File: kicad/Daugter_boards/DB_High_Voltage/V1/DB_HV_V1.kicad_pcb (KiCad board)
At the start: 2 copper layers, 57.2 x 50.8 mm, 38 parts, among them P1 CONN_01X19, P2 CONN_01X02, P3 CONN_01X19, P4 SMA, Q1 QN2222, Q2 QN2222, Q3 Q2N2907, U1 LM555N

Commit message: update DB_HV, update librairy and librairy path for MDL
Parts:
- Q1, Q2: value QN2222 -> Q2N2222
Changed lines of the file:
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@@
     (links 66)
     (no_connects 0)
-    (area 71.044999 30.526666 131.905 90.835001)
+    (area 71.044999 32.944999 128.345001 83.895001)
     (thickness 1.6)
     (drawings 4)
@@
     (pad_to_mask_clearance 0.2)
     (aux_axis_origin 0 0)
-    (visible_elements FFFFFF7F)
+    (visible_elements 7FFFFFFF)
     (pcbplotparams
       (layerselection 0x00030_80000001)
@@
       (effects (font (size 1 1) (thickness 0.15)))
     )
-    (fp_text value QN2222 (at 0 4.826 90) (layer F.Fab)
+    (fp_text value Q2N2222 (at 0 4.826 90) (layer F.Fab)
       (effects (font (size 1 1) (thickness 0.15)))
     )
@@
       (effects (font (size 1 1) (thickness 0.15)))
     )
-    (fp_text value QN2222 (at 0 4.826 90) (layer F.Fab)
-      (effects (font (size 1 1) (thickness 0.15)))
-    )
+    (fp_text value Q2N2222 (at 0 4.826 90) (layer F.Fab)
+      (effects (font (size 1 1) (thickness 0.15)))
+    )

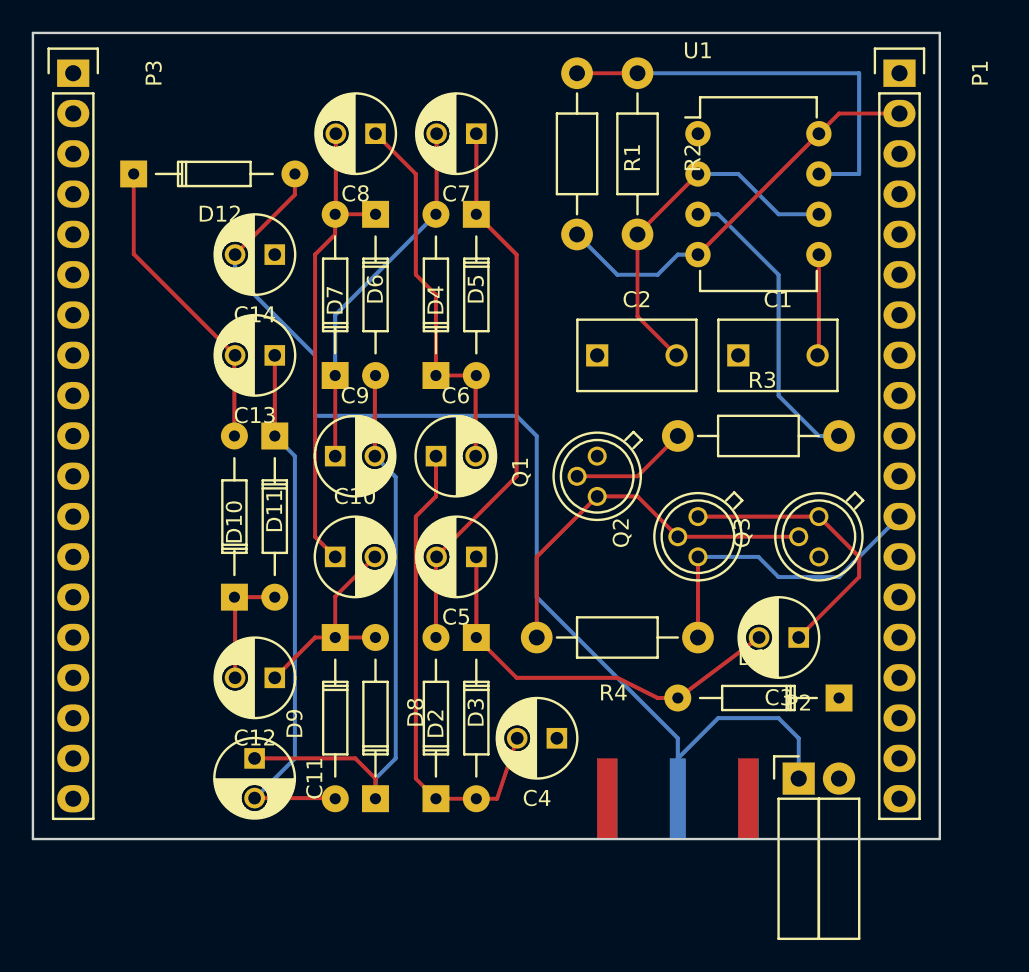
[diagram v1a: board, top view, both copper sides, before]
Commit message: inverting SMA layer position and improve finish of DB_HV
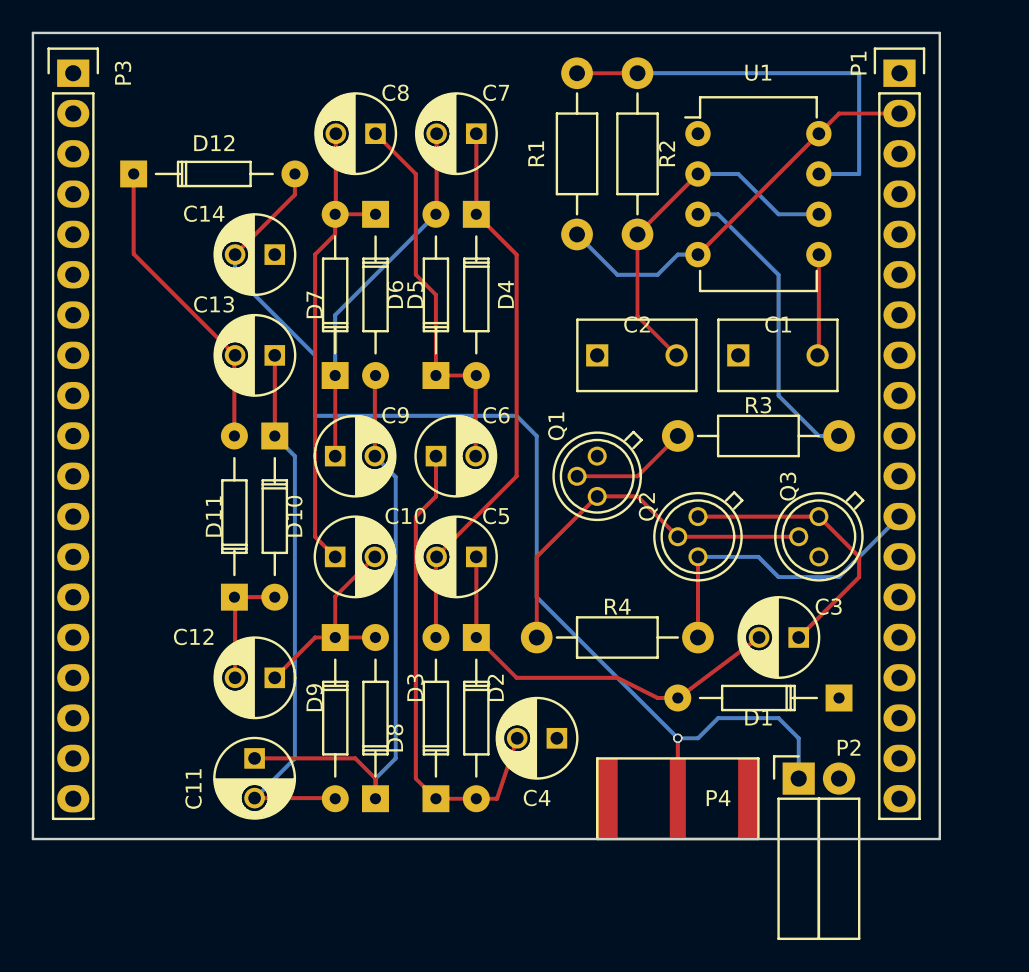
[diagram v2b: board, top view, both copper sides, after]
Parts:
- P4: moved to F.Cu
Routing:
- net Net-(C14-Pad2): track 74.2 -> 71.2 mm, vias 0 -> 1
